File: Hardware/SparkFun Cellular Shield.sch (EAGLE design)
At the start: 29 parts, among them U1 ARDUINO_R3_SHIELD, U2 SPX29302, U3 SM5100B, U4 SIMHOLDER3

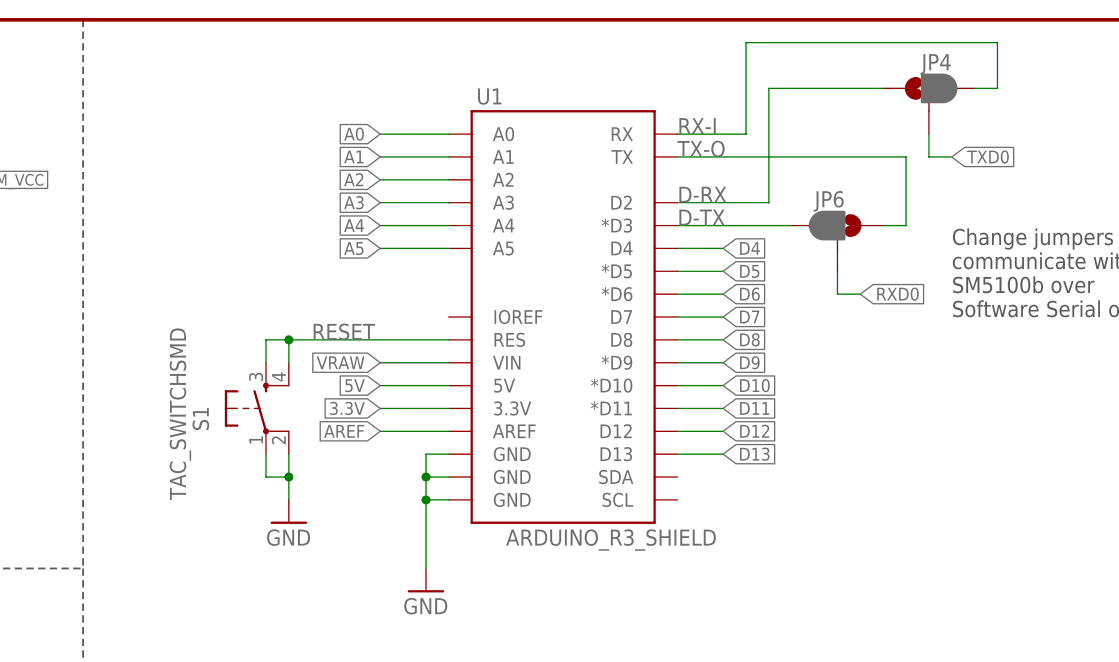
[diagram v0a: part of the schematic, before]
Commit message: Board layout cleanup
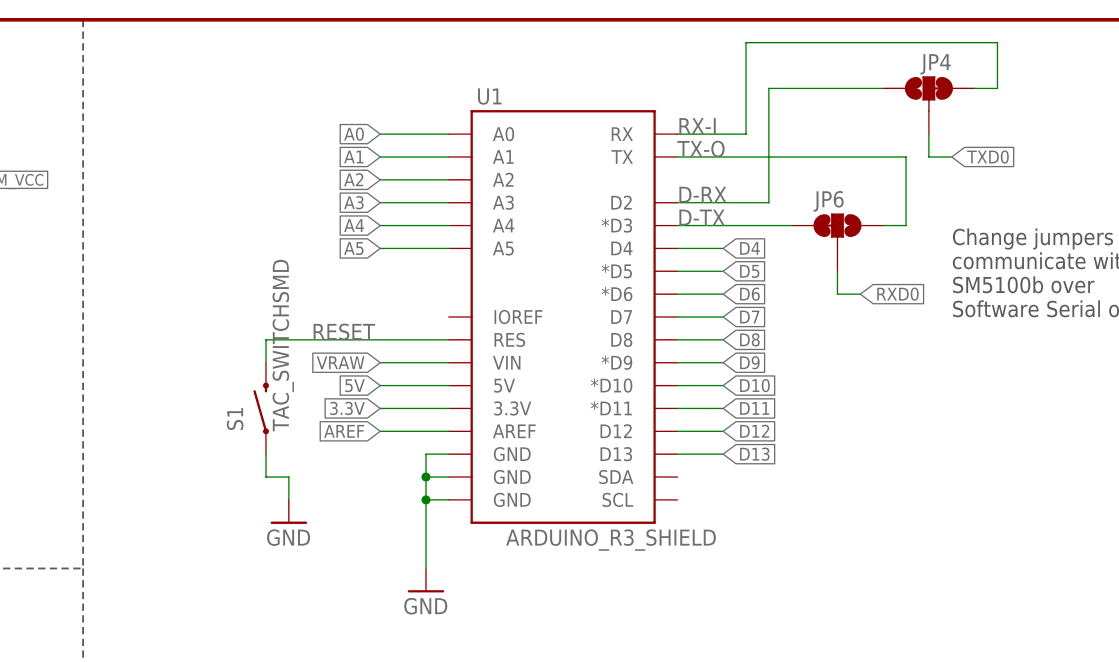
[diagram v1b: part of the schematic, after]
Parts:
- JP4, JP6: value JUMPER-PAD-3-2OF3_NC_BY_PASTE -> JUMPER-PAD-3-2OF3_NC_BY_TRACE_SMALL; device SparkFun-Passives:JUMPER-PAD-3-2OF3_NC_BY_PASTE -> SparkFun-Passives:JUMPER-PAD-3-2OF3_NC_BY_TRACE_SMALL
- S1: device SparkFun-Electromechanical:TAC_SWITCHSMD -> SparkFun-Electromechanical:SWITCH-MOMENTARY-2SMD
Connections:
- net GND: no longer S1.2
- net RESET: now also S1.2; no longer S1.3, S1.4
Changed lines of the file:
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@@
 <part name="R6" library="SparkFun-Resistors" deviceset="330OHM1/10W1%(0603)" device="" value="330"/>
 <part name="GND8" library="SparkFun-Aesthetics" deviceset="GND" device=""/>
-<part name="S1" library="SparkFun-Electromechanical" deviceset="TAC_SWITCH" device="SMD" value="TAC_SWITCHSMD"/>
+<part name="S1" library="SparkFun-Electromechanical" deviceset="SWITCH-MOMENTARY-2" device="SMD" value="TAC_SWITCHSMD"/>
 <part name="GND2" library="SparkFun-Aesthetics" deviceset="GND" device=""/>
-<part name="JP4" library="SparkFun-Passives" deviceset="JUMPER-PAD-3-2OF3_NC_BY_PASTE" device=""/>
-<part name="JP6" library="SparkFun-Passives" deviceset="JUMPER-PAD-3-2OF3_NC_BY_PASTE" device=""/>
+<part name="JP4" library="SparkFun-Passives" deviceset="JUMPER-PAD-3-2OF3_NC_BY_TRACE" device="_SMALL"/>
+<part name="JP6" library="SparkFun-Passives" deviceset="JUMPER-PAD-3-2OF3_NC_BY_TRACE" device="_SMALL"/>
 <part name="GND4" library="SparkFun-Aesthetics" deviceset="GND" device=""/>
 <part name="U$1" library="SparkFun-Aesthetics" deviceset="REVISION" device=""/>
@@
 <instance part="R6" gate="G$1" x="223.52" y="68.58" rot="R90"/>
 <instance part="GND8" gate="1" x="223.52" y="53.34"/>
-<instance part="S1" gate="S" x="137.16" y="142.24" smashed="yes" rot="R90">
-<attribute name="NAME" x="130.81" y="139.7" size="1.778" layer="95" rot="R90"/>
-<attribute name="VALUE" x="128.27" y="132.08" size="1.778" layer="96" rot="R90"/>
-</instance>
+<instance part="S1" gate="G$1" x="137.16" y="142.24" rot="R90"/>
 <instance part="GND2" gate="1" x="139.7" y="129.54"/>
 <instance part="JP4" gate="G$1" x="210.82" y="177.8" smashed="yes" rot="R90">
@@
 </segment>
 <segment>
-<wire x1="139.7" y1="137.16" x2="139.7" y2="134.62" width="0.1524" layer="91"/>
 <wire x1="139.7" y1="134.62" x2="139.7" y2="132.08" width="0.1524" layer="91"/>
 <wire x1="137.16" y1="137.16" x2="137.16" y2="134.62" width="0.1524" layer="91"/>
 <wire x1="137.16" y1="134.62" x2="139.7" y2="134.62" width="0.1524" layer="91"/>
-<junction x="139.7" y="134.62"/>
-<pinref part="S1" gate="S" pin="2"/>
-<pinref part="S1" gate="S" pin="1"/>
+<pinref part="S1" gate="G$1" pin="1"/>
 <pinref part="GND2" gate="1" pin="GND"/>
 </segment>
@@
 </segment>
 <segment>
-<wire x1="157.48" y1="149.86" x2="139.7" y2="149.86" width="0.1524" layer="91"/>
-<wire x1="139.7" y1="149.86" x2="139.7" y2="147.32" width="0.1524" layer="91"/>
-<wire x1="139.7" y1="149.86" x2="137.16" y2="149.86" width="0.1524" layer="91"/>
+<wire x1="157.48" y1="149.86" x2="137.16" y2="149.86" width="0.1524" layer="91"/>
 <wire x1="137.16" y1="149.86" x2="137.16" y2="147.32" width="0.1524" layer="91"/>
-<junction x="139.7" y="149.86"/>
 <label x="142.24" y="149.86" size="1.778" layer="95"/>
 <pinref part="U1" gate="G$1" pin="RES"/>
-<pinref part="S1" gate="S" pin="4"/>
-<pinref part="S1" gate="S" pin="3"/>
-</segment>
-</net>
+<pinref part="S1" gate="G$1" pin="2"/>
+</segment>
+</net>

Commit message: Additional part updates, adding dimensions
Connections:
- net GND: now also JP7.2
- net VCC: no longer JP7.2
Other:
- note added: "Ryan Owens"
- note removed: "Nathan Seidle"
- moved on the sheet: JP7
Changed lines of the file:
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@@
 <part name="STANDOFF1" library="SparkFun-Electromechanical" deviceset="STAND-OFF" device=""/>
 <part name="STANDOFF2" library="SparkFun-Electromechanical" deviceset="STAND-OFF" device=""/>
+<part name="GND11" library="SparkFun-Aesthetics" deviceset="GND" device=""/>
 </parts>
 <sheets>
@@
 <text x="238.76" y="7.62" size="2.54" layer="94">v13</text>
 <text x="175.26" y="7.62" size="2.54" layer="94">Toni Klopfenstein</text>
-<text x="171.45" y="11.43" size="2.54" layer="94">Nathan Seidle</text>
+<text x="171.45" y="11.43" size="2.54" layer="94">Ryan Owens</text>
 <wire x1="114.3" y1="185.42" x2="116.84" y2="185.42" width="0.2032" layer="97" style="longdash"/>
 <wire x1="116.84" y1="185.42" x2="116.84" y2="124.46" width="0.2032" layer="97" style="longdash"/>
@@
 <attribute name="VALUE" x="6.35" y="171.958" size="1.778" layer="96"/>
 </instance>
-<instance part="JP7" gate="G$1" x="15.24" y="88.9"/>
+<instance part="JP7" gate="G$1" x="15.24" y="88.9" rot="MR180"/>
 <instance part="STANDOFF1" gate="G$1" x="246.38" y="30.48"/>
 <instance part="STANDOFF2" gate="G$1" x="243.84" y="30.48"/>
+<instance part="GND11" gate="1" x="25.4" y="81.28"/>
 </instances>
 <busses>
@@
 <pinref part="GND10" gate="1" pin="GND"/>
 </segment>
+<segment>
+<pinref part="JP7" gate="G$1" pin="2"/>
+<wire x1="22.86" y1="86.36" x2="25.4" y2="86.36" width="0.1524" layer="91"/>
+<wire x1="25.4" y1="86.36" x2="25.4" y2="83.82" width="0.1524" layer="91"/>
+<pinref part="GND11" gate="1" pin="GND"/>
+</segment>
 </net>
 <net name="VCC" class="0">
@@
 <pinref part="U3" gate="G$1" pin="VBAT@2"/>
 <pinref part="U3" gate="G$1" pin="VBAT@3"/>
-<pinref part="JP7" gate="G$1" pin="2"/>
-<wire x1="22.86" y1="91.44" x2="30.48" y2="91.44" width="0.1524" layer="91"/>
-<junction x="30.48" y="91.44"/>
-</segment>
-<segment>
+</segment>
+<segment>

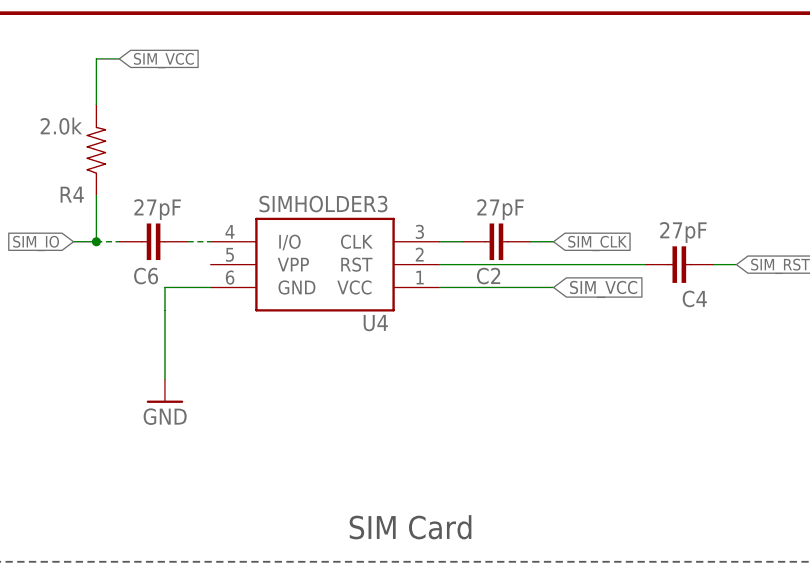
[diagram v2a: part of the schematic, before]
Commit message: Updating parts with PROD IDs, fixing DRC errors w/ tKeepout on
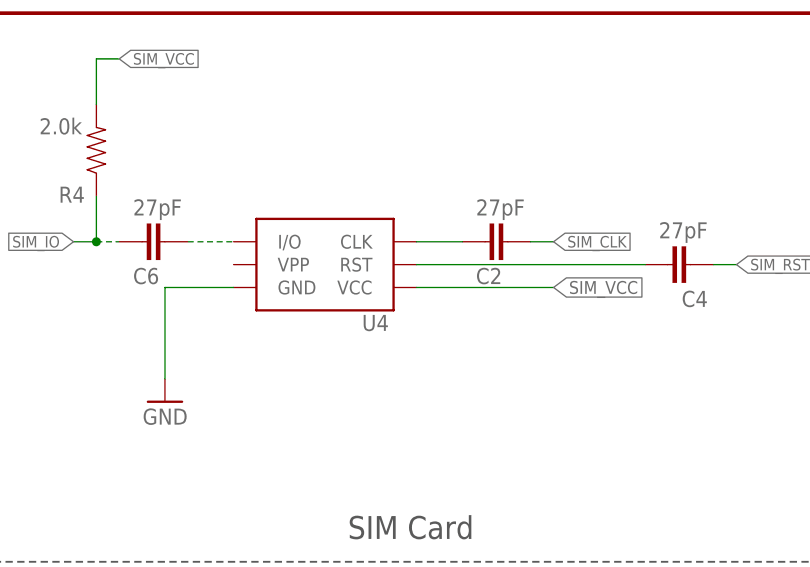
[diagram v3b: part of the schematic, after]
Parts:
- JP2, JP3: device SparkFun:FIDUCIAL1X2 -> SparkFun-Aesthetics:FIDUCIAL1X2
- R2, R3: device SparkFun-Resistors:10KOHM1/10W1%(0603)0603 -> SparkFun-Resistors:10KOHM-1/10W-1%(0603)0603
- U3: device SparkFun:SM5100B -> SparkFun-RF:SM5100B
- U4: value SIMHOLDER3 -> (none); device SparkFun:SIMHOLDER3 -> SparkFun-Connectors:SIMHOLDERSIM
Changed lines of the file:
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@@
 <part name="FRAME1" library="SparkFun-Aesthetics" deviceset="FRAME-LETTER" device=""/>
 <part name="JP1" library="SparkFun-Aesthetics" deviceset="SFE_LOGO_NAME_FLAME" device=".2_INCH"/>
-<part name="JP2" library="SparkFun" deviceset="FIDUCIAL" device="1X2"/>
-<part name="JP3" library="SparkFun" deviceset="FIDUCIAL" device="1X2"/>
+<part name="JP2" library="SparkFun-Aesthetics" deviceset="FIDUCIAL" device="1X2"/>
+<part name="JP3" library="SparkFun-Aesthetics" deviceset="FIDUCIAL" device="1X2"/>
 <part name="U1" library="SparkFun-Boards" deviceset="ARDUINO_R3_SHIELD" device=""/>
 <part name="GND3" library="SparkFun-Aesthetics" deviceset="GND" device=""/>
 <part name="P+2" library="SparkFun" deviceset="VCC" device=""/>
-<part name="R3" library="SparkFun-Resistors" deviceset="10KOHM1/10W1%(0603)" device="0603" value="10K"/>
+<part name="R3" library="SparkFun-Resistors" deviceset="10KOHM-1/10W-1%(0603)" device="0603" value="10K"/>
 <part name="P+4" library="SparkFun-Aesthetics" deviceset="VCC" device=""/>
-<part name="U4" library="SparkFun" deviceset="SIMHOLDER3" device=""/>
+<part name="U4" library="SparkFun-Connectors" deviceset="SIMHOLDER" device="SIM"/>
 <part name="GND9" library="SparkFun-Aesthetics" deviceset="GND" device=""/>
 <part name="JP5" library="SparkFun-Connectors" deviceset="M05" device="PTH"/>
 <part name="GND14" library="SparkFun-Aesthetics" deviceset="GND" device=""/>
-<part name="U3" library="SparkFun" deviceset="SM5100B" device=""/>
+<part name="U3" library="SparkFun-RF" deviceset="SM5100B" device=""/>
 <part name="C5" library="SparkFun-Capacitors" deviceset="100UF-10V-10%(TANT)" device="" value="100uF"/>
 <part name="GND5" library="SparkFun-Aesthetics" deviceset="GND" device=""/>
 <part name="GND6" library="SparkFun-Aesthetics" deviceset="GND" device=""/>
 <part name="R1" library="SparkFun-Resistors" deviceset="22KOHM1/10W1%(0603)" device="" value="22K"/>
-<part name="R2" library="SparkFun-Resistors" deviceset="10KOHM1/10W1%(0603)" device="0603" value="10K"/>
+<part name="R2" library="SparkFun-Resistors" deviceset="10KOHM-1/10W-1%(0603)" device="0603" value="10K"/>
 <part name="GND7" library="SparkFun-Aesthetics" deviceset="GND" device=""/>
 <part name="GND1" library="SparkFun-Aesthetics" deviceset="GND" device=""/>
@@
 <instance part="R3" gate="G$1" x="22.86" y="27.94" rot="MR0"/>
 <instance part="P+4" gate="G$1" x="12.7" y="30.48" rot="MR0"/>
-<instance part="U4" gate="G$1" x="38.1" y="157.48" rot="R180"/>
+<instance part="U4" gate="J1" x="38.1" y="157.48" rot="R180"/>
 <instance part="GND9" gate="1" x="20.32" y="142.24" rot="MR0"/>
 <instance part="JP5" gate="G$1" x="106.68" y="96.52" rot="R180"/>
@@
 </segment>
 <segment>
-<wire x1="25.4" y1="154.94" x2="20.32" y2="154.94" width="0.1524" layer="91"/>
-<wire x1="20.32" y1="154.94" x2="20.32" y2="152.4" width="0.1524" layer="91"/>
-<wire x1="20.32" y1="152.4" x2="20.32" y2="144.78" width="0.1524" layer="91"/>
-<pinref part="U4" gate="G$1" pin="GND"/>
+<wire x1="27.94" y1="154.94" x2="20.32" y2="154.94" width="0.1524" layer="91"/>
+<wire x1="20.32" y1="154.94" x2="20.32" y2="144.78" width="0.1524" layer="91"/>
+<pinref part="U4" gate="J1" pin="GND"/>
 <pinref part="GND9" gate="1" pin="GND"/>
 </segment>
@@
 <net name="SIM_VCC" class="0">
 <segment>
-<wire x1="50.8" y1="154.94" x2="63.5" y2="154.94" width="0.1524" layer="91"/>
-<pinref part="U4" gate="G$1" pin="VCC"/>
+<wire x1="48.26" y1="154.94" x2="63.5" y2="154.94" width="0.1524" layer="91"/>
+<pinref part="U4" gate="J1" pin="VCC"/>
 <label x="63.5" y="154.94" size="1.4224" layer="95" xref="yes"/>
 </segment>
@@
 <segment>
 <pinref part="C6" gate="G$1" pin="1"/>
-<pinref part="U4" gate="G$1" pin="I/O"/>
-<wire x1="22.86" y1="160.02" x2="25.4" y2="160.02" width="0.1524" layer="91" style="longdash"/>
+<pinref part="U4" gate="J1" pin="I/O"/>
+<wire x1="22.86" y1="160.02" x2="27.94" y2="160.02" width="0.1524" layer="91" style="longdash"/>
 </segment>
 </net>
 <net name="N$2" class="0">
 <segment>
-<pinref part="U4" gate="G$1" pin="RST"/>
+<pinref part="U4" gate="J1" pin="RST"/>
 <pinref part="C4" gate="G$1" pin="2"/>
-<wire x1="50.8" y1="157.48" x2="73.66" y2="157.48" width="0.1524" layer="91"/>
+<wire x1="48.26" y1="157.48" x2="73.66" y2="157.48" width="0.1524" layer="91"/>
 </segment>
 </net>
 <net name="N$3" class="0">
 <segment>
-<pinref part="U4" gate="G$1" pin="CLK"/>
+<pinref part="U4" gate="J1" pin="CLK"/>
 <pinref part="C2" gate="G$1" pin="2"/>
-<wire x1="50.8" y1="160.02" x2="53.34" y2="160.02" width="0.1524" layer="91"/>
-</segment>
-</net>
+<wire x1="48.26" y1="160.02" x2="53.34" y2="160.02" width="0.1524" layer="91"/>
+</segment>
+</net>

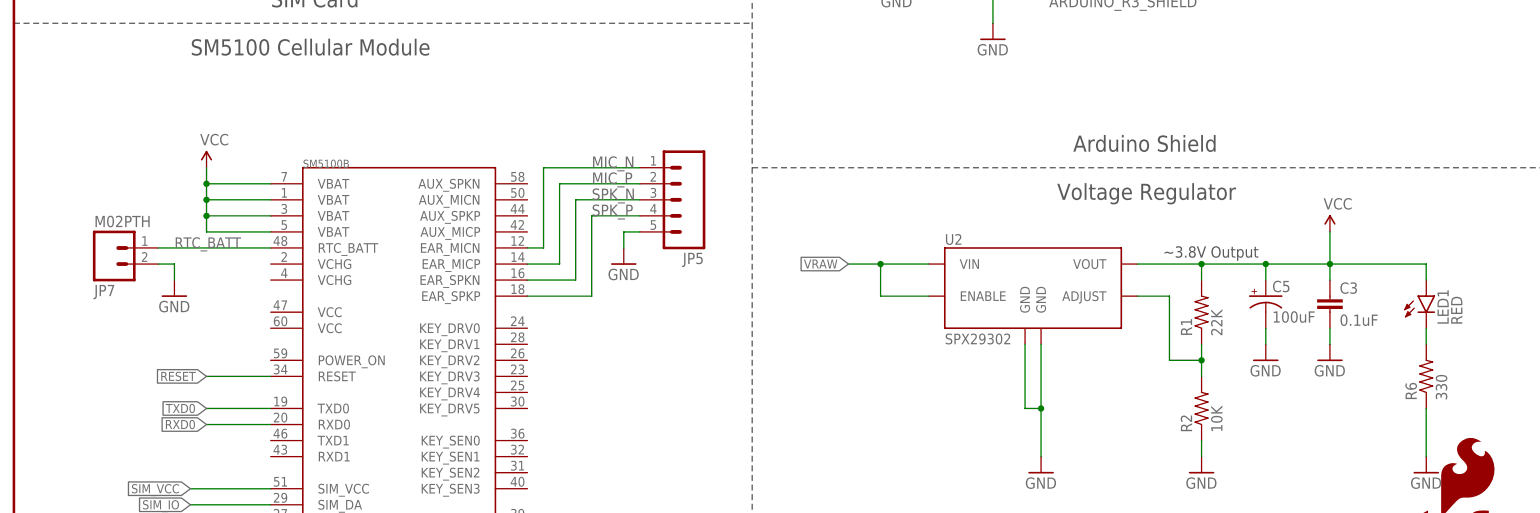
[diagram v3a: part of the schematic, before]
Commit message: Adding in 20mm battery fp for RTC
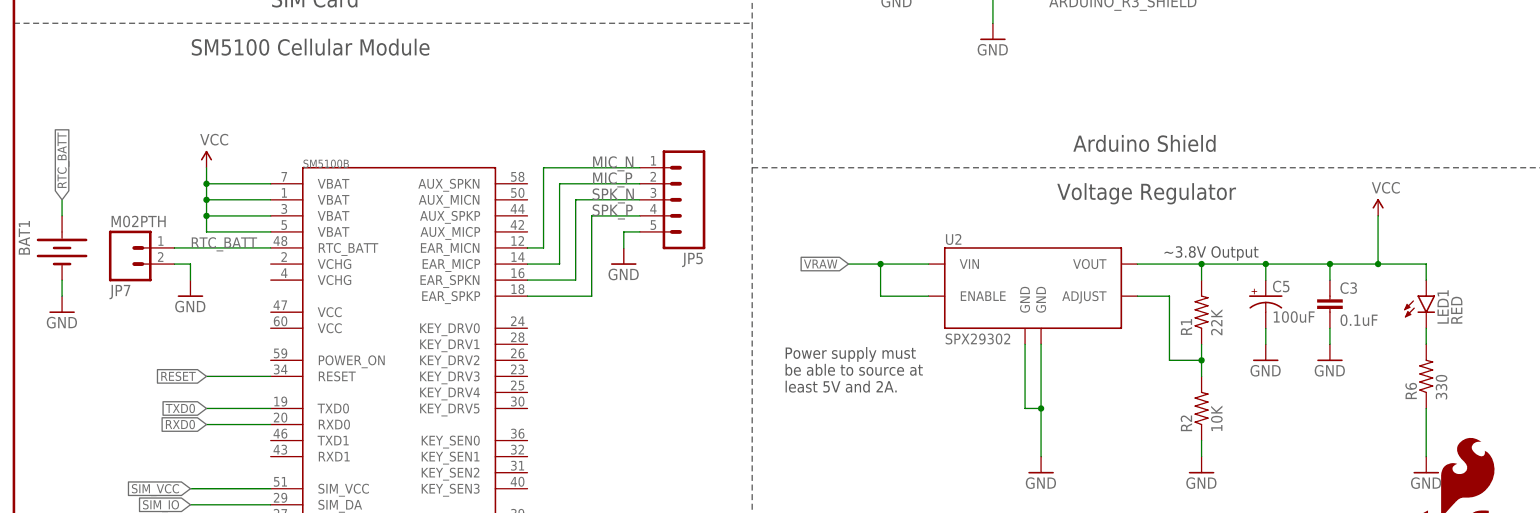
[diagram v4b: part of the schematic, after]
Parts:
- added BAT1: (no value), SparkFun-Electromechanical:BATTERY20PTH
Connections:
- net GND: now also BAT1.-
- net RTC_BATT: now also BAT1.+
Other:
- note added: "Power supply must be able to source at least 5V and 2A."
- moved on the sheet: JP7
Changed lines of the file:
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@@
 <part name="STANDOFF2" library="SparkFun-Electromechanical" deviceset="STAND-OFF" device=""/>
 <part name="GND11" library="SparkFun-Aesthetics" deviceset="GND" device=""/>
+<part name="BAT1" library="SparkFun-Electromechanical" deviceset="BATTERY" device="20PTH"/>
+<part name="GND12" library="SparkFun-Aesthetics" deviceset="GND" device=""/>
 </parts>
 <sheets>
@@
 <text x="167.64" y="104.14" size="2.54" layer="97">Arduino Shield</text>
 <text x="165.1" y="96.52" size="2.54" layer="97">Voltage Regulator</text>
+<text x="121.92" y="66.04" size="1.778" layer="97">Power supply must
+be able to source at
+least 5V and 2A.</text>
 </plain>
 <instances>
@@
 <instance part="C3" gate="G$1" x="208.28" y="78.74"/>
 <instance part="LED1" gate="G$1" x="223.52" y="81.28"/>
-<instance part="P+1" gate="G$1" x="208.28" y="91.44"/>
+<instance part="P+1" gate="G$1" x="215.9" y="93.98"/>
 <instance part="R6" gate="G$1" x="223.52" y="68.58" rot="R90"/>
 <instance part="GND8" gate="1" x="223.52" y="53.34"/>
@@
 <attribute name="VALUE" x="6.35" y="171.958" size="1.778" layer="96"/>
 </instance>
-<instance part="JP7" gate="G$1" x="15.24" y="88.9" rot="MR180"/>
+<instance part="JP7" gate="G$1" x="17.78" y="88.9" rot="MR180"/>
 <instance part="STANDOFF1" gate="G$1" x="246.38" y="30.48"/>
 <instance part="STANDOFF2" gate="G$1" x="243.84" y="30.48"/>
-<instance part="GND11" gate="1" x="25.4" y="81.28"/>
+<instance part="GND11" gate="1" x="27.94" y="81.28"/>
+<instance part="BAT1" gate="G$1" x="7.62" y="88.9" smashed="yes" rot="R270">
+<attribute name="NAME" x="2.54" y="87.63" size="1.778" layer="95" rot="R90"/>
+<attribute name="VALUE" x="1.27" y="92.71" size="1.778" layer="96" rot="R270"/>
+</instance>
+<instance part="GND12" gate="1" x="7.62" y="78.74"/>
 </instances>
 <busses>
@@
 <segment>
 <pinref part="JP7" gate="G$1" pin="2"/>
-<wire x1="22.86" y1="86.36" x2="25.4" y2="86.36" width="0.1524" layer="91"/>
-<wire x1="25.4" y1="86.36" x2="25.4" y2="83.82" width="0.1524" layer="91"/>
+<wire x1="25.4" y1="86.36" x2="27.94" y2="86.36" width="0.1524" layer="91"/>
+<wire x1="27.94" y1="86.36" x2="27.94" y2="83.82" width="0.1524" layer="91"/>
 <pinref part="GND11" gate="1" pin="GND"/>
+</segment>
+<segment>
+<pinref part="BAT1" gate="G$1" pin="-"/>
+<wire x1="7.62" y1="83.82" x2="7.62" y2="81.28" width="0.1524" layer="91"/>
+<pinref part="GND12" gate="1" pin="GND"/>
 </segment>
 </net>
@@
 <wire x1="187.96" y1="86.36" x2="198.12" y2="86.36" width="0.1524" layer="91"/>
 <wire x1="187.96" y1="86.36" x2="187.96" y2="83.82" width="0.1524" layer="91"/>
-<wire x1="208.28" y1="86.36" x2="208.28" y2="91.44" width="0.1524" layer="91"/>
-<wire x1="208.28" y1="86.36" x2="223.52" y2="86.36" width="0.1524" layer="91"/>
+<wire x1="208.28" y1="86.36" x2="215.9" y2="86.36" width="0.1524" layer="91"/>
+<wire x1="215.9" y1="86.36" x2="223.52" y2="86.36" width="0.1524" layer="91"/>
 <wire x1="223.52" y1="86.36" x2="223.52" y2="83.82" width="0.1524" layer="91"/>
 <junction x="198.12" y="86.36"/>
@@
 <pinref part="R1" gate="G$1" pin="2"/>
 <pinref part="C3" gate="G$1" pin="1"/>
+<pinref part="LED1" gate="G$1" pin="A"/>
 <pinref part="P+1" gate="G$1" pin="VCC"/>
-<pinref part="LED1" gate="G$1" pin="A"/>
+<wire x1="215.9" y1="93.98" x2="215.9" y2="86.36" width="0.1524" layer="91"/>
+<junction x="215.9" y="86.36"/>
 </segment>
 </net>
@@
 <segment>
 <pinref part="U3" gate="G$1" pin="RTC_BATT"/>
-<wire x1="40.64" y1="88.9" x2="22.86" y2="88.9" width="0.1524" layer="91"/>
+<wire x1="40.64" y1="88.9" x2="25.4" y2="88.9" width="0.1524" layer="91"/>
 <pinref part="JP7" gate="G$1" pin="1"/>
-<label x="25.4" y="88.9" size="1.6764" layer="95"/>
-</segment>
-</net>
+<label x="27.94" y="88.9" size="1.6764" layer="95"/>
+</segment>
+<segment>
+<pinref part="BAT1" gate="G$1" pin="+"/>
+<wire x1="7.62" y1="96.52" x2="7.62" y2="93.98" width="0.1524" layer="91"/>
+<label x="7.62" y="96.52" size="1.4224" layer="95" rot="R90" xref="yes"/>
+</segment>
+</net>
